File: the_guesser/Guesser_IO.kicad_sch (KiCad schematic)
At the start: 5 parts, among them J4 Screw_Terminal_01x06, J5 Screw_Terminal_01x06, J7 USB_C_Receptacle_USB2.0_16P, U6 FUSB307BMPX, U7 TPD4S014

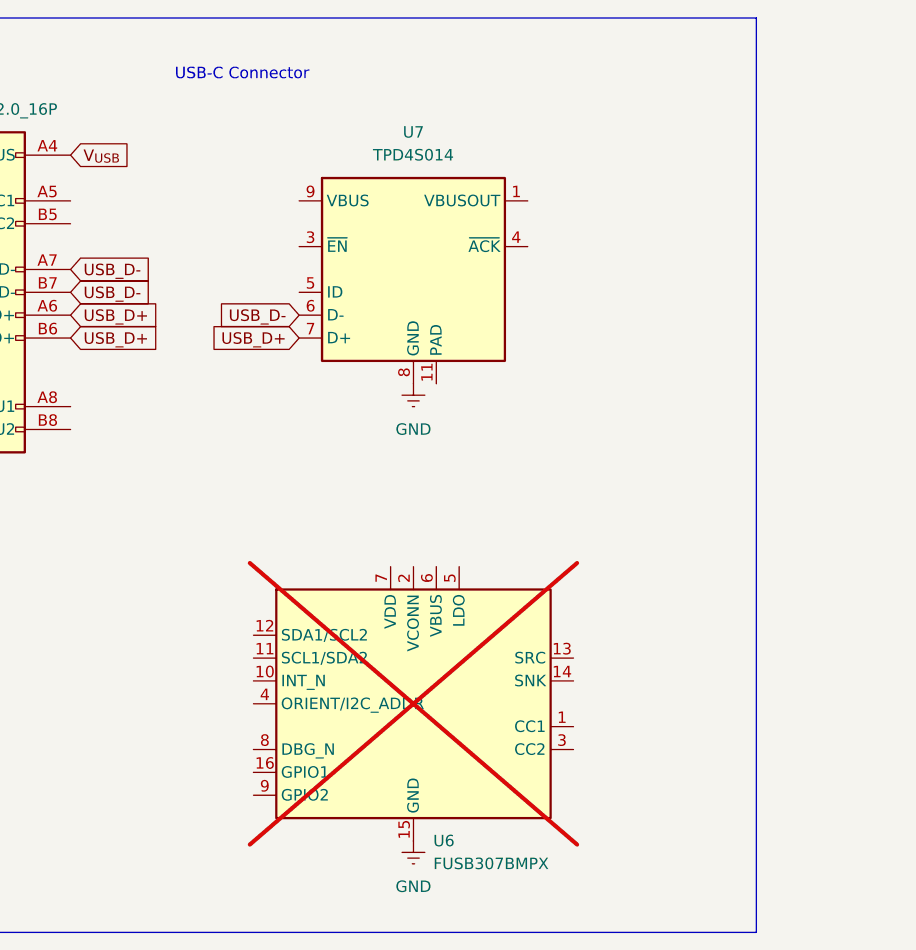
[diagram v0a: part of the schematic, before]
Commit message: Finished Guesser sensor selection and started sensor routing
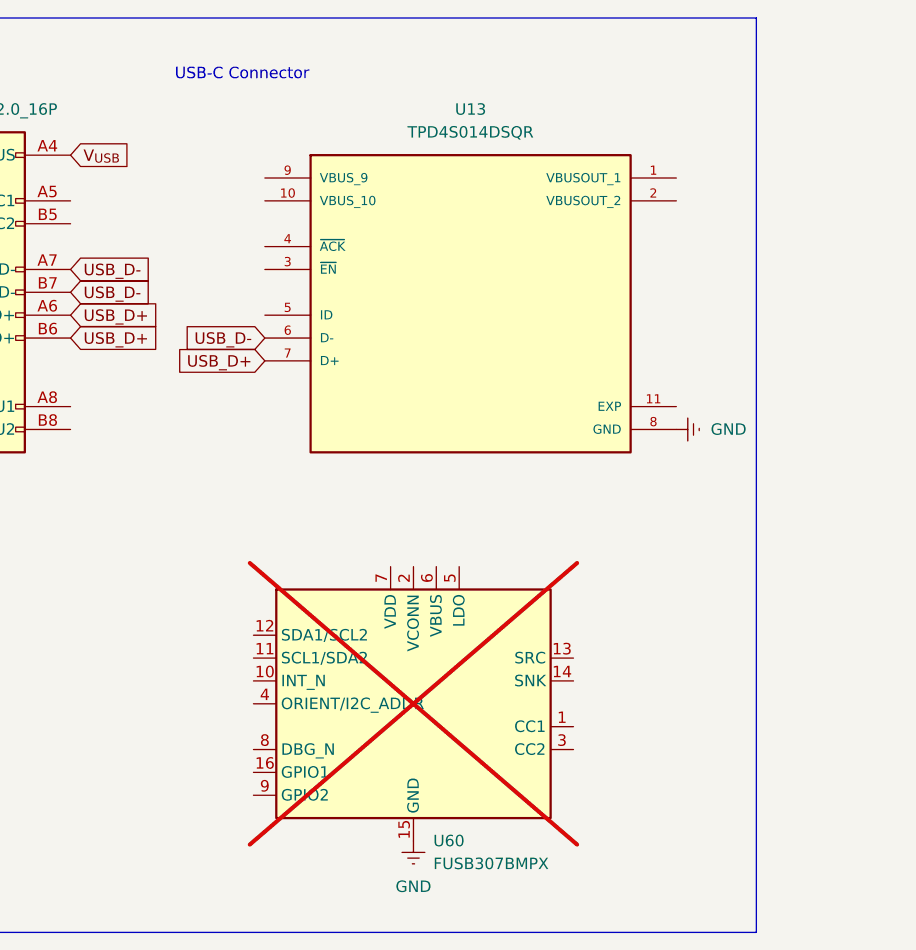
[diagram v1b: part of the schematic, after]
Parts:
- removed U7: TPD4S014, Package_SON:Texas_S-PWSON-N10, symbol Power_Protection:TPD4S014
- added U13: TPD4S014DSQR, locals_but_working_PLEASE:TPD4S014DSQR, symbol Custom_Flight_Computer_Symbols:TPD4S014DSQR
- renumbered U6 to U60
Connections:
- net GND: now also U13.8 (GND)
- net USB_D+: now also U13.7 (D+)
- net USB_D-: now also U13.6 (D-)
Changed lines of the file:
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@@
 	(global_label "USB_D+"
 		(shape input)
-		(at 76.2 48.26 180)
+		(at 72.39 50.8 180)
 		(fields_autoplaced yes)
 		(effects
@@
 		)
 		(property "Intersheetrefs" "${INTERSHEET_REFS}"
-			(at 65.5948 48.26 0)
+			(at 61.7848 50.8 0)
 			(effects
 				(font
@@
 	(global_label "USB_D-"
 		(shape input)
-		(at 76.2 45.72 180)
+		(at 72.39 48.26 180)
 		(fields_autoplaced yes)
 		(effects
@@
 		)
 		(property "Intersheetrefs" "${INTERSHEET_REFS}"
-			(at 65.5948 45.72 0)
+			(at 61.7848 48.26 0)
 			(effects
 				(font
@@
 		(dnp yes)
 		(fields_autoplaced yes)
-		(property "Reference" "U6"
+		(property "Reference" "U60"
 			(at 91.0941 104.14 0)
 			(effects
@@
 			(project "the_guesser"
 				(path "/473e3a2e-6c5e-4995-af4a-e4bf1449cab0/0bcaec57-f6d5-41f0-b678-342e153337b7"
-					(reference "U6")
+					(reference "U60")
 					(unit 1)
 				)
@@
 	)
 	(symbol
+		(lib_id "Custom_Flight_Computer_Symbols:TPD4S014DSQR")
+		(at 95.25 45.72 0)
+		(unit 1)
+		(exclude_from_sim no)
+		(in_bom yes)
+		(on_board yes)
+		(dnp no)
+		(fields_autoplaced yes)
+		(property "Reference" "U13"
+			(at 95.25 22.86 0)
+			(effects
+				(font
+					(size 1.27 1.27)
+				)
+			)
+		)
+		(property "Value" "TPD4S014DSQR"
+			(at 95.25 25.4 0)
+			(effects
+				(font
+					(size 1.27 1.27)
+				)
+			)
+		)
+		(property "Footprint" "locals_but_working_PLEASE:TPD4S014DSQR"
+			(at 95.25 45.72 0)
+			(effects
+				(font
+					(size 1.27 1.27)
+				)
+				(justify bottom)
+				(hide yes)
+			)
+		)
+		(property "Datasheet" "https://www.ti.com/lit/ds/symlink/tpd4s014.pdf?HQS=dis-dk-null-digikeymode-dsf-pf-null-wwe&ts=1716147734171&ref_url=https%253A%252F%252Fwww.ti.com%252Fgeneral%252Fdocs%252Fsuppproductinfo.tsp%253FdistId%253D10%2526gotoUrl%253Dhttps%253A%252F%252Fwww.ti.com%252Flit%252Fgpn%252Ftpd4s014"
+			(at 95.25 45.72 0)
+			(effects
+				(font
+					(size 1.27 1.27)
+				)
+				(hide yes)
+			)
+		)
+		(property "Description" "  Overvoltage Protection Controller 10-WSON (2x2)"
+			(at 95.25 45.72 0)
+			(effects
+				(font
+					(size 1.27 1.27)
+				)
+				(hide yes)
+			)
+		)
+		(property "PARTREV" "E"
+			(at 95.25 45.72 0)
+			(effects
+				(font
+					(size 1.27 1.27)
+				)
+				(justify bottom)
+				(hide yes)
+			)
+		)
+		(property "STANDARD" "IPC-7351B"
+			(at 95.25 45.72 0)
+			(effects
+				(font
+					(size 1.27 1.27)
+				)
+				(justify bottom)
+				(hide yes)
+			)
+		)
+		(property "MAXIMUM_PACKAGE_HEIGHT" "0.8mm"
+			(at 95.25 45.72 0)
+			(effects
+				(font
+					(size 1.27 1.27)
+				)
+				(justify bottom)
+				(hide yes)
+			)
+		)
+		(property "MANUFACTURER" "Texas Instruments"
+			(at 95.25 45.72 0)
+			(effects
+				(font
+					(size 1.27 1.27)
+				)
+				(justify bottom)
+				(hide yes)
+			)
+		)
+		(property "DKPN" "296-29093-1-ND"
+			(at 95.25 45.72 0)
+			(effects
+				(font
+					(size 1.27 1.27)
+				)
+				(hide yes)
+			)
+		)
+		(pin "8"
+		)
+		(pin "3"
+		)
+		(pin "11"
+		)
+		(pin "10"
+		)
+		(pin "5"
+		)
+		(pin "9"
+		)
+		(pin "7"
+		)
+		(pin "4"
+		)
+		(pin "2"
+		)
+		(pin "1"
+		)
+		(pin "6"
+		)
+		(instances
+			(project "the_guesser"
+				(path "/473e3a2e-6c5e-4995-af4a-e4bf1449cab0/0bcaec57-f6d5-41f0-b678-342e153337b7"
+					(reference "U13")
+					(unit 1)
+				)
+			)
+		)
+	)
+	(symbol
 		(lib_id "Connector:Screw_Terminal_01x06")
 		(at 254 30.48 0)
@@
 	)
 	(symbol
-		(lib_id "Power_Protection:TPD4S014")
-		(at 88.9 40.64 0)
-		(unit 1)
-		(exclude_from_sim no)
-		(in_bom yes)
-		(on_board yes)
-		(dnp no)
-		(fields_autoplaced yes)
-		(property "Reference" "U7"
-			(at 88.9 25.4 0)
-			(effects
-				(font
-					(size 1.27 1.27)
-				)
-			)
-		)
-		(property "Value" "TPD4S014"
-			(at 88.9 27.94 0)
-			(effects
-				(font
-					(size 1.27 1.27)
-				)
-			)
-		)
-		(property "Footprint" "Package_SON:Texas_S-PWSON-N10"
-			(at 111.76 53.34 0)
-			(effects
-				(font
-					(size 1.27 1.27)
-				)
-				(hide yes)
-			)
-		)
-		(property "Datasheet" "http://www.ti.com/lit/ds/symlink/tpd4s014.pdf"
-			(at 116.84 58.42 0)
-			(effects
-				(font
-					(size 1.27 1.27)
-				)
-				(hide yes)
-			)
-		)
-		(property "Description" "USB Charger Port Protection Including ESD Protection for All Lines and Overvoltage Protection on VBUS"
-			(at 88.9 40.64 0)
-			(effects
-				(font
-					(size 1.27 1.27)
-				)
-				(hide yes)
-			)
-		)
-		(pin "5"
-		)
-		(pin "6"
-		)
-		(pin "7"
-		)
-		(pin "10"
-		)
-		(pin "3"
-		)
-		(pin "11"
-		)
-		(pin "9"
-		)
-		(pin "1"
-		)
-		(pin "8"
-		)
-		(pin "2"
-		)
-		(pin "4"
-		)
-		(instances
-			(project "the_guesser"
-				(path "/473e3a2e-6c5e-4995-af4a-e4bf1449cab0/0bcaec57-f6d5-41f0-b678-342e153337b7"
-					(reference "U7")
-					(unit 1)
-				)
-			)
-		)
-	)
-	(symbol
 		(lib_id "Connector:USB_C_Receptacle_USB2.0_16P")
 		(at 35.56 43.18 0)
@@
 	(symbol
 		(lib_id "power:Earth")
-		(at 88.9 53.34 0)
+		(at 118.11 58.42 90)
 		(unit 1)
 		(exclude_from_sim no)
@@
 		(fields_autoplaced yes)
 		(property "Reference" "#PWR047"
-			(at 88.9 59.69 0)
+			(at 124.46 58.42 0)
 			(effects
 				(font
@@
 		)
 		(property "Value" "GND"
-			(at 88.9 58.42 0)
-			(effects
-				(font
-					(size 1.27 1.27)
-				)
+			(at 121.92 58.4199 90)
+			(effects
+				(font
+					(size 1.27 1.27)
+				)
+				(justify right)
 			)
 		)
 		(property "Footprint" ""
-			(at 88.9 53.34 0)
+			(at 118.11 58.42 0)
 			(effects
 				(font
@@
 		)
 		(property "Datasheet" "~"
-			(at 88.9 53.34 0)
+			(at 118.11 58.42 0)
 			(effects
 				(font
@@
 		)
 		(property "Description" "Power symbol creates a global label with name \"Earth\""
-			(at 88.9 53.34 0)
-			(effects
-				(font
+			(at 118.11 58.42 0)
+			(effects
+				(font

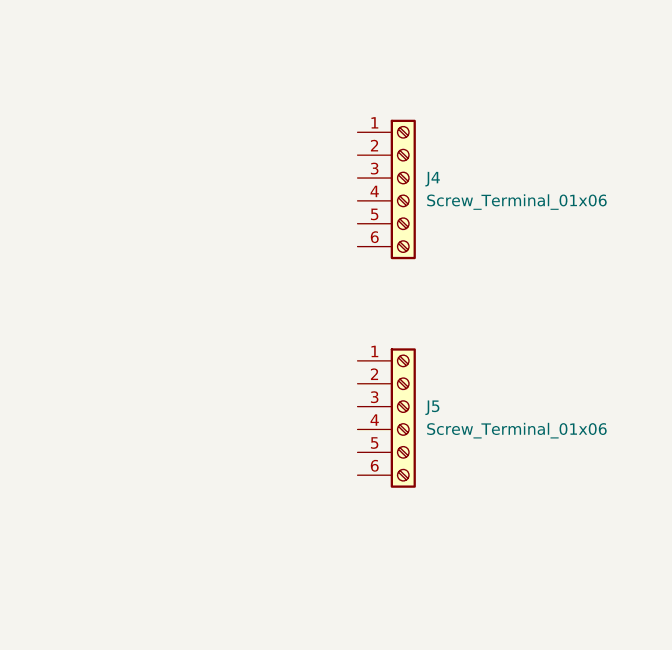
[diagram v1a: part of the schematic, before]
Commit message: Routed USB and SPI buses
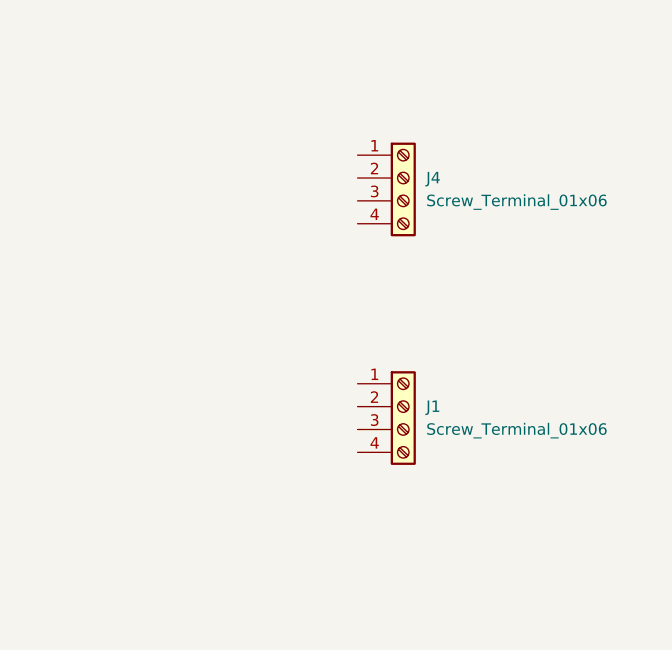
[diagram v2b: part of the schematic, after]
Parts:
- removed J5: Screw_Terminal_01x06, TerminalBlock_Phoenix:TerminalBlock_Phoenix_MPT-0,5-6-2.54_1x06_P2.54mm_Horizontal, symbol Connector:Screw_Terminal_01x06
- added J1: Screw_Terminal_01x06, TerminalBlock_Phoenix:TerminalBlock_Phoenix_MPT-0,5-4-2.54_1x04_P2.54mm_Horizontal, symbol Connector:Screw_Terminal_01x04
- J4: footprint TerminalBlock_Phoenix:TerminalBlock_Phoenix_MPT-0,5-6-2.54_1x06_P2.54mm_Horizontal -> TerminalBlock_Phoenix:TerminalBlock_Phoenix_MPT-0,5-4-2.54_1x04_P2.54mm_Horizontal; symbol Connector:Screw_Terminal_01x06 -> Connector:Screw_Terminal_01x04
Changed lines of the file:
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@@
 	)
 	(symbol
-		(lib_id "Connector:Screw_Terminal_01x06")
+		(lib_id "Connector:Screw_Terminal_01x04")
 		(at 254 30.48 0)
 		(unit 1)
@@
 			)
 		)
-		(property "Footprint" "TerminalBlock_Phoenix:TerminalBlock_Phoenix_MPT-0,5-6-2.54_1x06_P2.54mm_Horizontal"
+		(property "Footprint" "TerminalBlock_Phoenix:TerminalBlock_Phoenix_MPT-0,5-4-2.54_1x04_P2.54mm_Horizontal"
 			(at 254 30.48 0)
 			(effects
@@
 			)
 		)
-		(property "Description" "Generic screw terminal, single row, 01x06, script generated (kicad-library-utils/schlib/autogen/connector/)"
+		(property "Description" "Generic screw terminal, single row, 01x04, script generated (kicad-library-utils/schlib/autogen/connector/)"
 			(at 254 30.48 0)
 			(effects
@@
 		(pin "1"
 		)
-		(pin "6"
-		)
 		(pin "4"
 		)
 		(pin "2"
-		)
-		(pin "5"
 		)
 		(instances
@@
 	)
 	(symbol
+		(lib_id "Connector:Screw_Terminal_01x04")
+		(at 254 55.88 0)
+		(unit 1)
+		(exclude_from_sim no)
+		(in_bom yes)
+		(on_board yes)
+		(dnp no)
+		(fields_autoplaced yes)
+		(property "Reference" "J1"
+			(at 256.54 55.8799 0)
+			(effects
+				(font
+					(size 1.27 1.27)
+				)
+				(justify left)
+			)
+		)
+		(property "Value" "Screw_Terminal_01x06"
+			(at 256.54 58.4199 0)
+			(effects
+				(font
+					(size 1.27 1.27)
+				)
+				(justify left)
+			)
+		)
+		(property "Footprint" "TerminalBlock_Phoenix:TerminalBlock_Phoenix_MPT-0,5-4-2.54_1x04_P2.54mm_Horizontal"
+			(at 254 55.88 0)
+			(effects
+				(font
+					(size 1.27 1.27)
+				)
+				(hide yes)
+			)
+		)
+		(property "Datasheet" "~"
+			(at 254 55.88 0)
+			(effects
+				(font
+					(size 1.27 1.27)
+				)
+				(hide yes)
+			)
+		)
+		(property "Description" "Generic screw terminal, single row, 01x04, script generated (kicad-library-utils/schlib/autogen/connector/)"
+			(at 254 55.88 0)
+			(effects
+				(font
+					(size 1.27 1.27)
+				)
+				(hide yes)
+			)
+		)
+		(pin "3"
+		)
+		(pin "1"
+		)
+		(pin "4"
+		)
+		(pin "2"
+		)
+		(instances
+			(project "the_guesser"
+				(path "/473e3a2e-6c5e-4995-af4a-e4bf1449cab0/0bcaec57-f6d5-41f0-b678-342e153337b7"
+					(reference "J1")
+					(unit 1)
+				)
+			)
+		)
+	)
+	(symbol
 		(lib_id "power:Earth")
 		(at 118.11 58.42 90)
@@
 					(unit 1)
 				)
-			)
-		)
-	)
-	(symbol
-		(lib_id "Connector:Screw_Terminal_01x06")
-		(at 254 55.88 0)
-		(unit 1)
-		(exclude_from_sim no)
-		(in_bom yes)
-		(on_board yes)
-		(dnp no)
-		(fields_autoplaced yes)
-		(property "Reference" "J5"
-			(at 256.54 55.8799 0)
-			(effects
-				(font
-					(size 1.27 1.27)
-				)
-				(justify left)
-			)
-		)
-		(property "Value" "Screw_Terminal_01x06"
-			(at 256.54 58.4199 0)
-			(effects
-				(font
-					(size 1.27 1.27)
-				)
-				(justify left)
-			)
-		)
-		(property "Footprint" "TerminalBlock_Phoenix:TerminalBlock_Phoenix_MPT-0,5-6-2.54_1x06_P2.54mm_Horizontal"
-			(at 254 55.88 0)
-			(effects
-				(font
-					(size 1.27 1.27)
-				)
-				(hide yes)
-			)
-		)
-		(property "Datasheet" "~"
-			(at 254 55.88 0)
-			(effects
-				(font
-					(size 1.27 1.27)
-				)
-				(hide yes)
-			)
-		)
-		(property "Description" "Generic screw terminal, single row, 01x06, script generated (kicad-library-utils/schlib/autogen/connector/)"
-			(at 254 55.88 0)
-			(effects
-				(font
-					(size 1.27 1.27)
-				)
-				(hide yes)
-			)
-		)
-		(pin "3"
-		)
-		(pin "1"
-		)
-		(pin "6"
-		)
-		(pin "4"
-		)
-		(pin "2"
-		)
-		(pin "5"
-		)
-		(instances
-			(project "the_guesser"
-				(path "/473e3a2e-6c5e-4995-af4a-e4bf1449cab0/0bcaec57-f6d5-41f0-b678-342e153337b7"
-					(reference "J5")
-					(unit 1)
-				)

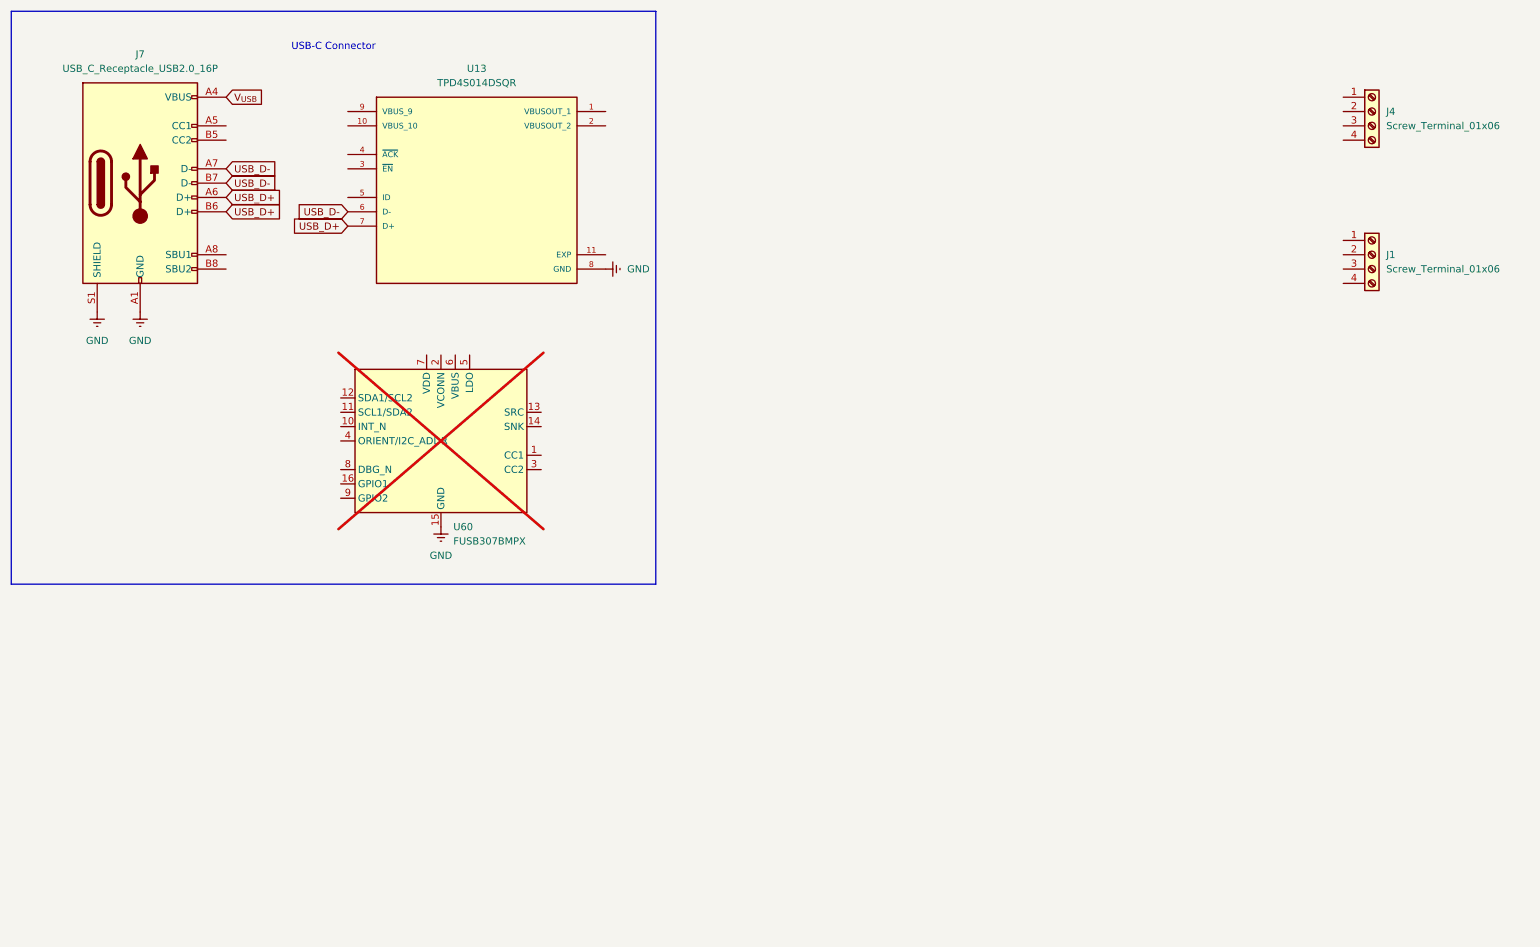
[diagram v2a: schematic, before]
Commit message: Routed Guesser pyro channels
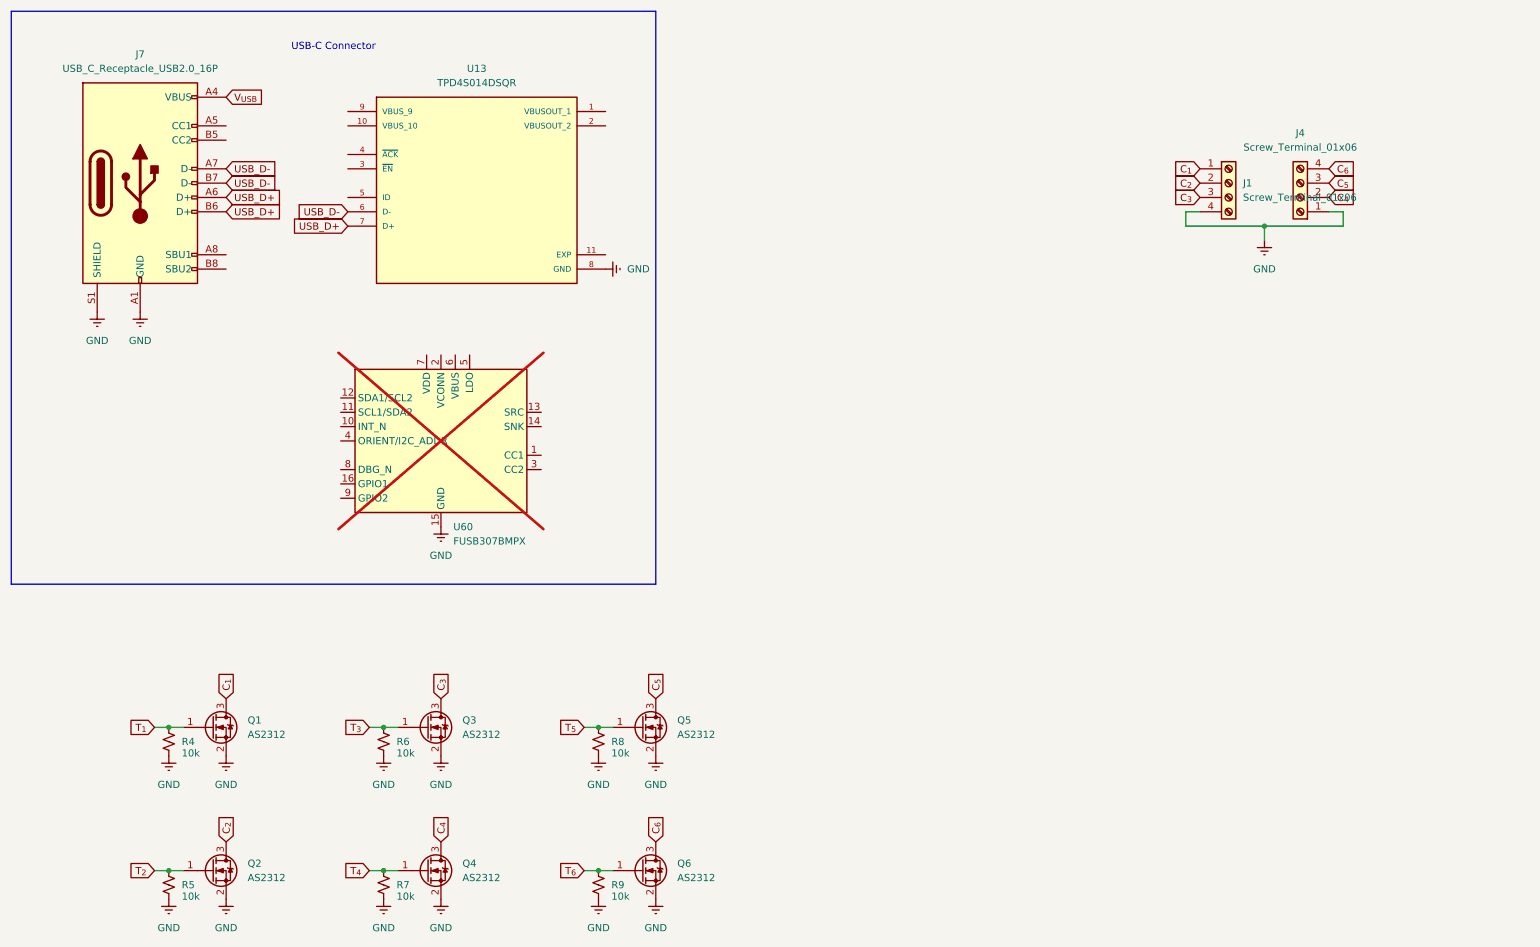
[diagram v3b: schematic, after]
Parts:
- added Q1, Q2, Q3, Q4, Q5, Q6: AS2312, Package_TO_SOT_SMD:SOT-23, symbol Transistor_FET:2N7002
- added R4, R5, R6, R7, R8, R9: 10k, Resistor_SMD:R_0603_1608Metric, symbol Device:R_Small_US
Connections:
- net GND: now also J1.4 (Pin_4), J4.1 (Pin_1), Q1.2 (S), Q2.2 (S), Q3.2 (S), Q4.2 (S), Q5.2 (S), Q6.2 (S), R4.2, R5.2, R6.2, R7.2, R8.2, R9.2
- net C_{4}: now reaches J4.2 (Pin_2)
- net C_{4}: now also Q4.3 (D)
- net C_{5}: now reaches J4.3 (Pin_3)
- net C_{5}: now also Q5.3 (D)
- net C_{6}: now reaches J4.4 (Pin_4)
- net C_{6}: now also Q6.3 (D)
- net C_{1}: now reaches J1.1 (Pin_1)
- net C_{1}: now also Q1.3 (D)
- net C_{2}: now reaches J1.2 (Pin_2)
- net C_{2}: now also Q2.3 (D)
- net C_{3}: now reaches J1.3 (Pin_3)
- net C_{3}: now also Q3.3 (D)
- new net T_{1}: Q1.1 (G), R4.1
- new net T_{2}: Q2.1 (G), R5.1
- new net T_{3}: Q3.1 (G), R6.1
- new net T_{4}: Q4.1 (G), R7.1
- new net T_{5}: Q5.1 (G), R8.1
- new net T_{6}: Q6.1 (G), R9.1
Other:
- moved on the sheet: J1, J4
